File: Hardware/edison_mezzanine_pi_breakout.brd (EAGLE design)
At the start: 30.5 x 44.5 mm, 44 parts, among them U1 PCA9306, U2 EDISON_CONNECTOR_FULLMOUNTING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, U3 EDISON_CONNECTOR_FULLHEADER, U4 TPS62065, U5 MIC5219 3.3V

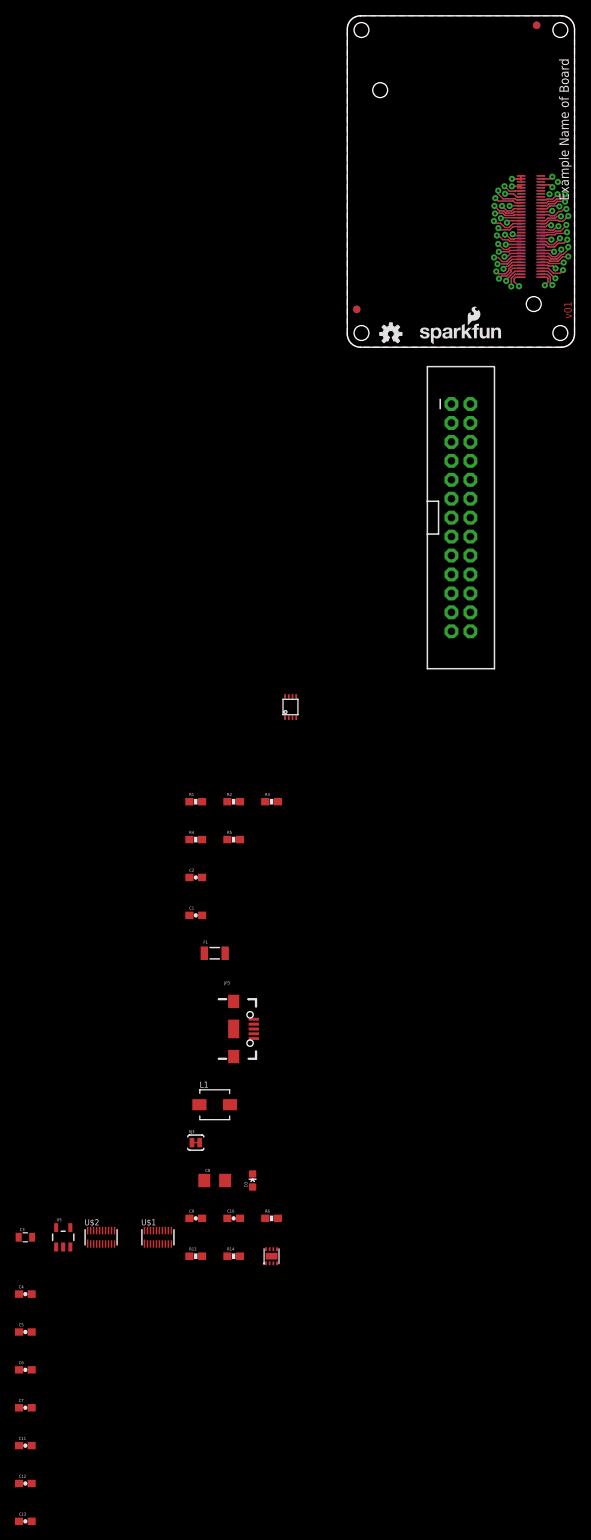
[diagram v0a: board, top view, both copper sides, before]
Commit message: Initial component placement.
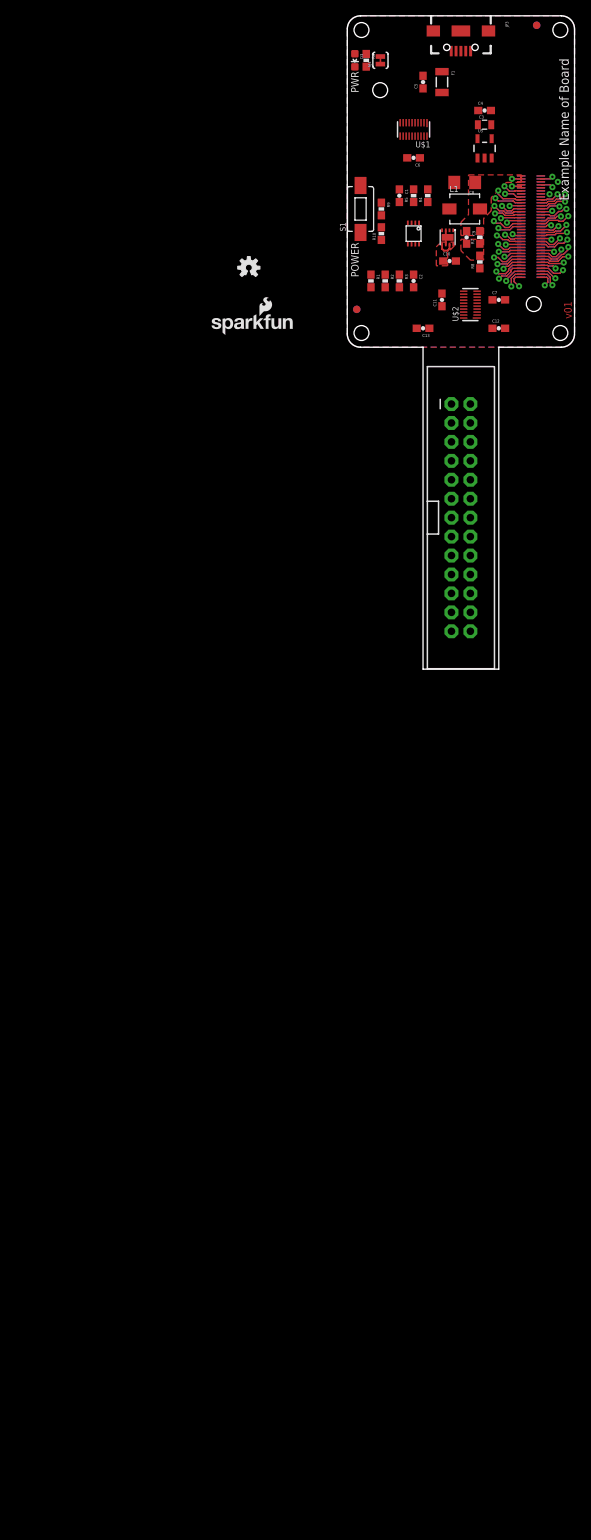
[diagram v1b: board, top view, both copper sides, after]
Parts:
- removed R13: 680k, SparkFun-Resistors:0603-RES
- removed R14: 120k, SparkFun-Resistors:0603-RES
- added R10: 22, SparkFun-Resistors:0603-RES
- added R7: 680k, SparkFun-Resistors:0603-RES
- added R8: 120k, SparkFun-Resistors:0603-RES
- added R9: 10K, SparkFun-Resistors:0603-RES
- added S1: POWER, SparkFun-Electromechanical:TACTILE-SWITCH-1101NE
- moved C5 175.9 mm to (10.2, 35.6), turned to 90 degrees
- moved C6 170.7 mm to (8.89, 25.4), turned to 180 degrees
- moved C4 170.3 mm to (18.4, 31.8)
- moved C13 168.7 mm to (10.2, 2.54), turned to 180 degrees
- moved C12 167.4 mm to (20.3, 2.54)
- moved C11 163.5 mm to (12.7, 6.35), turned to 90 degrees
- moved C7 161.6 mm to (20.3, 6.35)
- moved C3 161.4 mm to (18.4, 29.8)
- moved U5 156.6 mm to (18.4, 26.7)
- moved R6 155.8 mm to (2.54, 38.5), turned to 270 degrees
- moved U$1 152.5 mm to (8.89, 29.2), turned to 180 degrees
- moved D3 150.9 mm to (1.02, 38.5), turned to 180 degrees
- moved SJ3 147.3 mm to (4.45, 38.5), turned to 90 degrees
- moved U4 138.7 mm to (13.5, 14.7), turned to 180 degrees
- moved C8 138.0 mm to (15.7, 22.1), turned to 180 degrees
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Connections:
- new net N$15: R10.2, R9.2, S1.P$1
- net GND: now also R8.1, S1.P$2; no longer R14.1
- net N$18: now also R7.1, R8.2; no longer R13.1, R14.2
- net PWRBTN#: now also R10.1
- net VSYS: now also R7.2, R9.1; no longer R13.2
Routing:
- net 5V: track 0.00 -> 2.37 mm
- net GND: track 0.00 -> 2.11 mm
- added copper zone on layer 1, net 5V
- added copper zone on layer 1, net N$18
- added copper zone on layer 1, net VSYS
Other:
- board size 30.5 x 44.5 mm -> 30.5 x 87.6 mm
- board text added: "POWER"
- board text added: "PWR"
- board text added: "Shawn Hymel"
- board text removed: "Engineer"

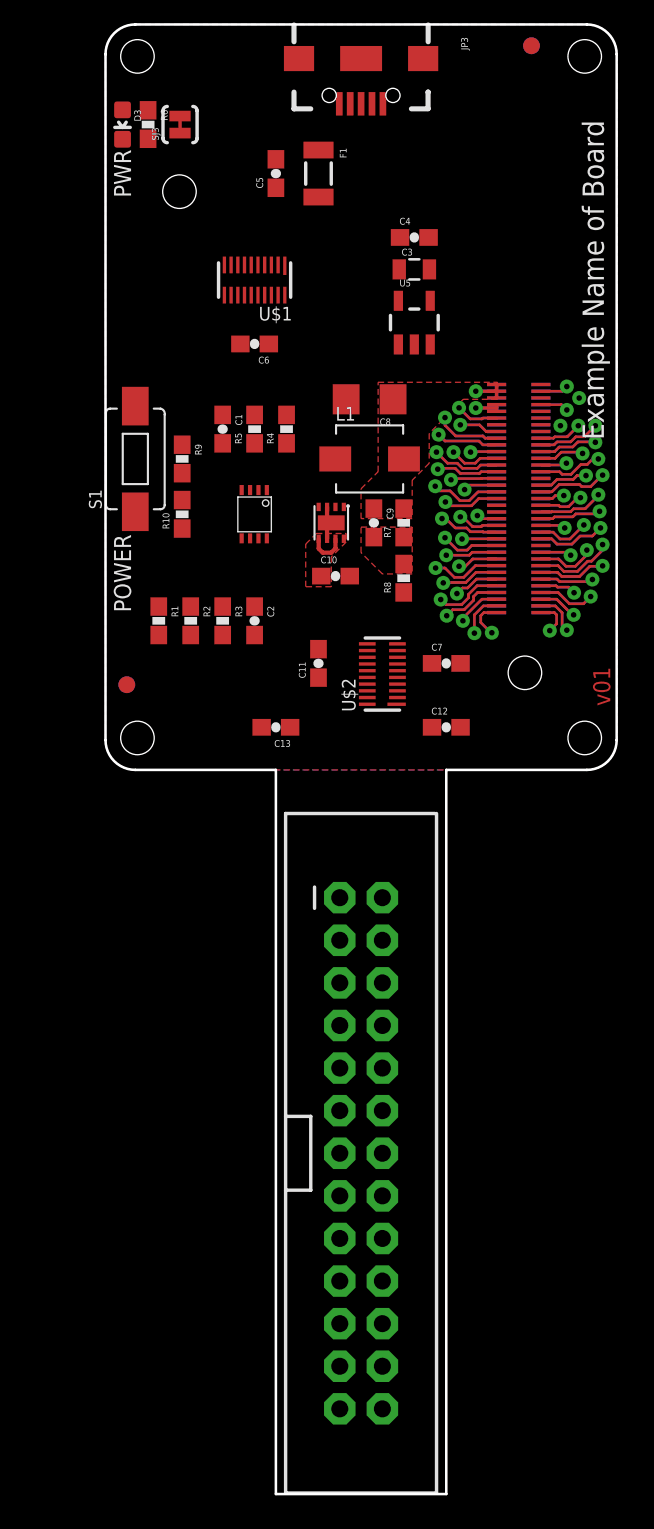
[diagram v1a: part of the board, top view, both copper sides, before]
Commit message: More layout. Swapped 22 Ohm with 220 Ohm in schematic for power button.
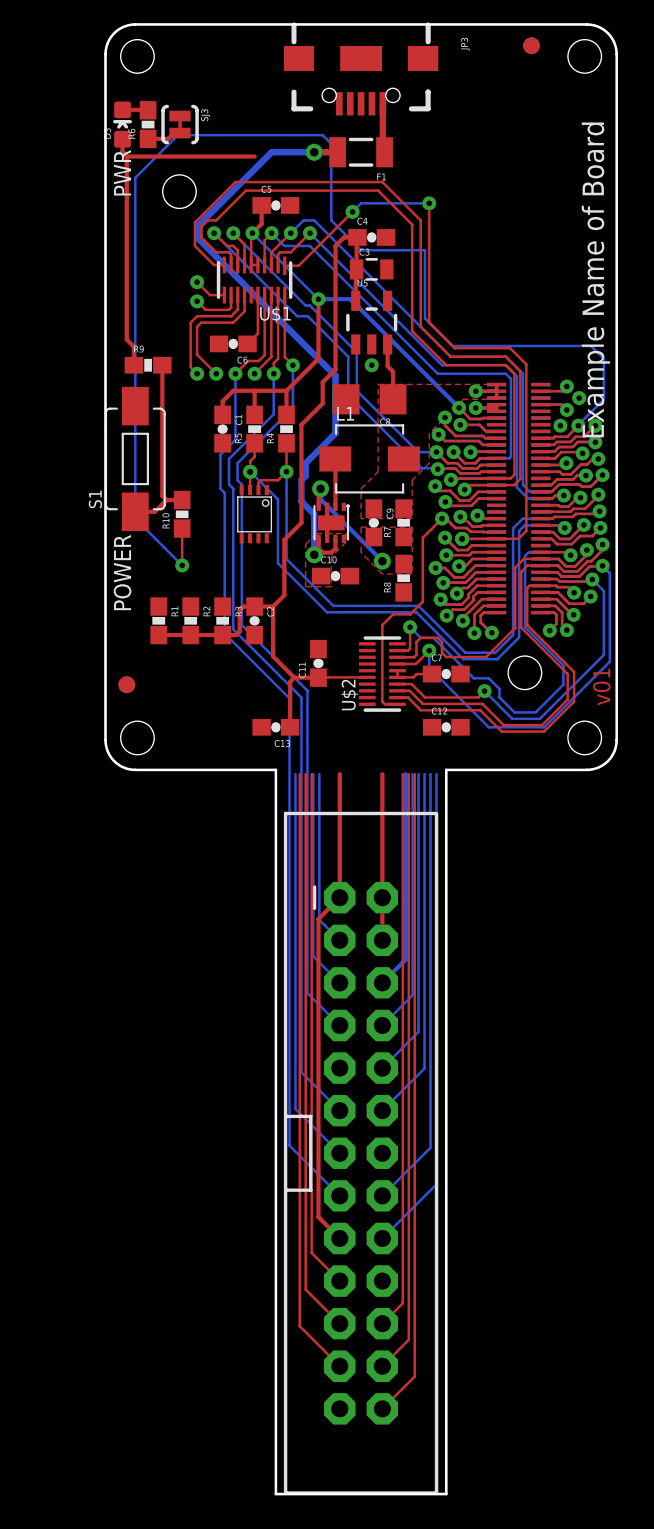
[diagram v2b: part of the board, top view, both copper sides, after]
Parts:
- R10: value 22 -> 220
- moved R9 5.95 mm to (2.54, 24.1), turned to 0 degrees
- moved F1 2.84 mm to (15.2, 36.8), turned to 180 degrees
- moved C3 2.54 mm to (15.9, 29.8)
- moved C4 2.54 mm to (15.9, 31.8)
- moved U5 2.54 mm to (15.9, 26.7)
- moved C5 1.91 mm to (10.2, 33.7), turned to 0 degrees
- moved C6 1.27 mm to (7.62, 25.4)
- moved C7 0.63 mm to (20.3, 5.71)
- turned D3 to 0 degrees
- turned R6 to 90 degrees
- turned SJ3 to 270 degrees
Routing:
- net 3.3V_LOCAL: track 0.00 -> 80.7 mm
- net PWRBTN#: track 5.08 -> 75.7 mm, vias 1 -> 2
- net PI_GP22: track 0.00 -> 58.1 mm, vias 0 -> 1
- net PI_GP17: track 0.00 -> 52.6 mm, vias 0 -> 1
- net PI_GP4: track 0.00 -> 47.6 mm, vias 0 -> 1
- net 5V: track 2.37 -> 46.5 mm, vias 0 -> 2
- net GP48: track 4.04 -> 44.5 mm
- net PI_CE1: track 0.00 -> 38.6 mm
- net GP47: track 5.51 -> 43.9 mm
- net 1.8V: track 5.07 -> 42.4 mm, vias 1 -> 3
- net PI_GP25: track 0.00 -> 36.3 mm, vias 0 -> 1
- net PI_SCLK: track 0.00 -> 36.3 mm
- net PI_GP24: track 0.00 -> 36.2 mm, vias 0 -> 1
- net GP14: track 4.13 -> 40.1 mm, vias 1 -> 4
- net PI_CE0: track 0.00 -> 36.0 mm
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
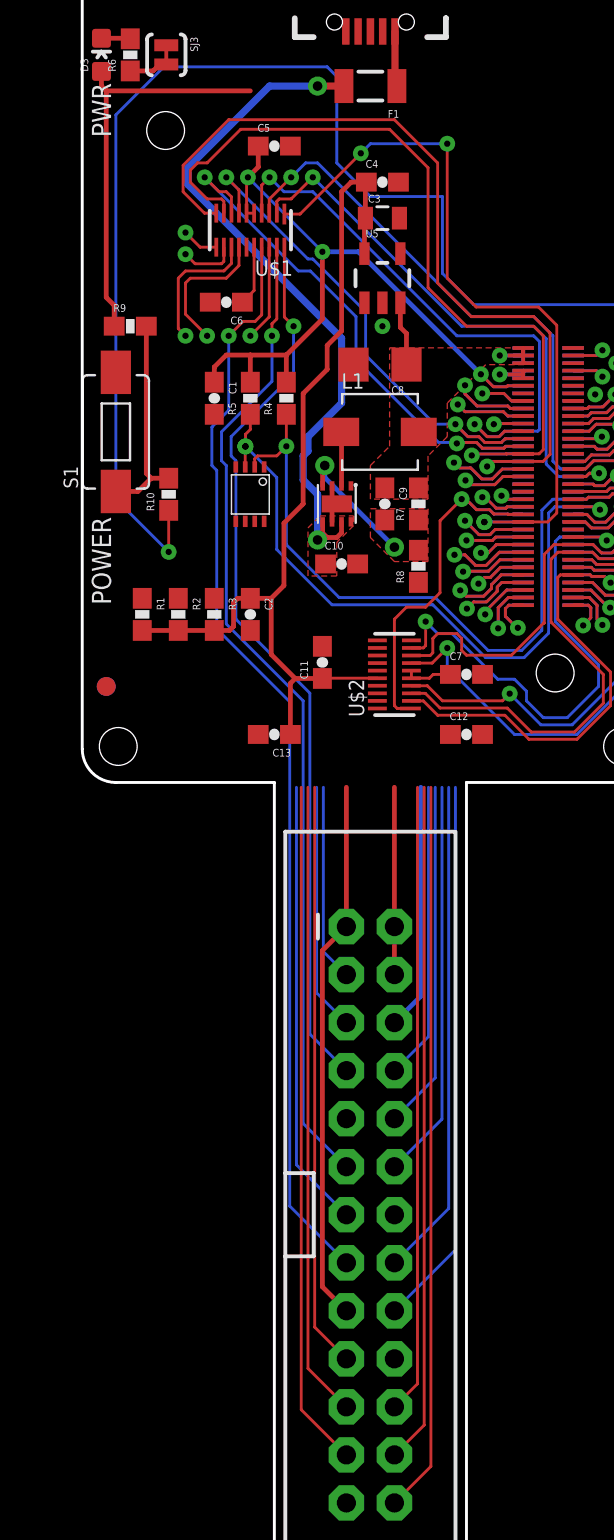
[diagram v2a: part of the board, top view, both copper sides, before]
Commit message: Added more layout to Pi connector.
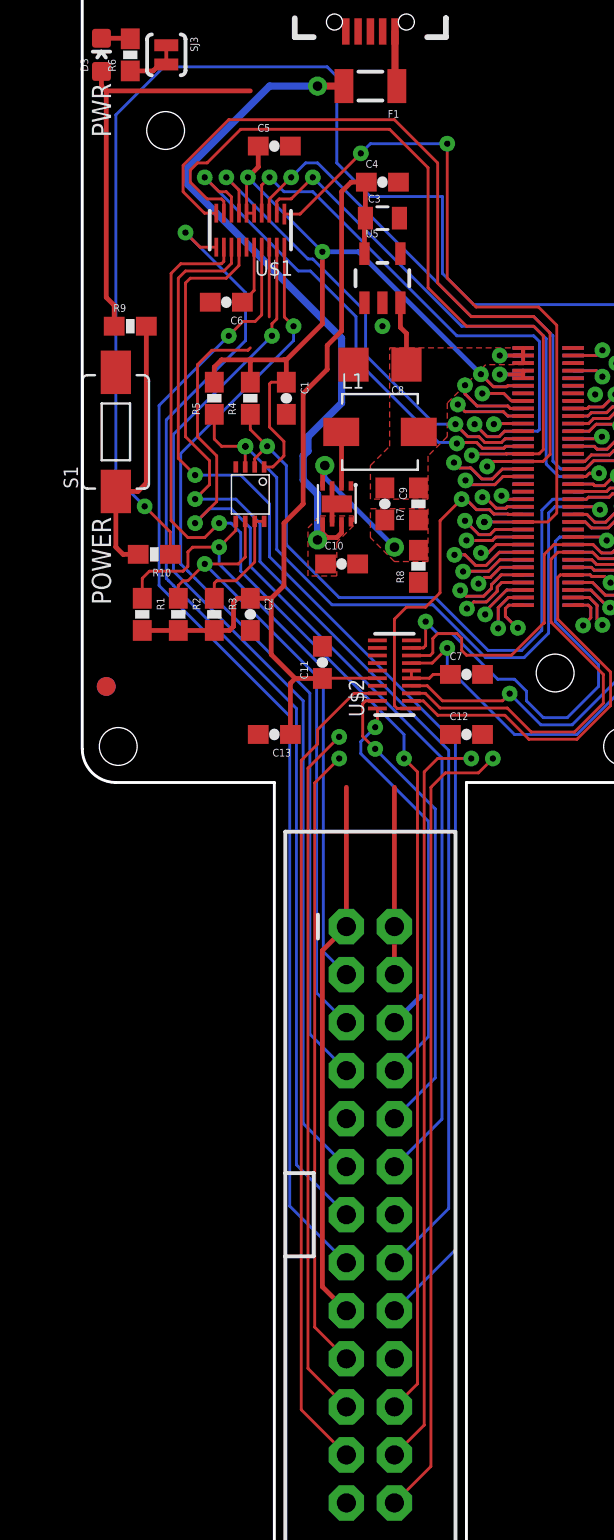
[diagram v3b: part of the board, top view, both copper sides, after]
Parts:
- moved C1 3.81 mm to (10.8, 20.3)
- moved R10 3.27 mm to (3.81, 12.1), turned to 180 degrees
- moved R5 1.91 mm to (6.99, 20.3)
- moved R4 1.90 mm to (8.89, 20.3)
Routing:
- net PI_GP25: track 36.3 -> 72.1 mm, vias 1 -> 2
- net PI_GP27: track 25.6 -> 60.9 mm
- net PI_GP18#: track 26.2 -> 58.8 mm
- net PI_GP24: track 36.2 -> 67.4 mm
- net PI_GP23: track 33.8 -> 64.8 mm
- net HV_SDA: track 10.4 -> 33.4 mm, vias 0 -> 1
- net HV_SCL: track 13.1 -> 34.1 mm, vias 0 -> 1
- net GND: track 15.1 -> 4.08 mm
- net PI_SCLK: track 36.3 -> 43.7 mm
- net PI_RXI: track 18.4 -> 25.3 mm, vias 0 -> 1
- net N$1: track 0.00 -> 6.05 mm
- net 1.8V: track 42.4 -> 48.5 mm
- net PI_TXO: track 15.7 -> 21.7 mm, vias 0 -> 1
- net PI_CE1: track 38.6 -> 42.6 mm, vias 0 -> 1
- net PI_CE0: track 36.0 -> 39.6 mm, vias 0 -> 1
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
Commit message: More layout.
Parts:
- moved C11 1.27 mm to (11.4, 6.35)
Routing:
- net 5V: track 46.5 -> 65.7 mm, vias 2 -> 4
- net PI_CE0: track 39.6 -> 55.5 mm, vias 1 -> 2
- net PI_CE1: track 42.6 -> 58.1 mm, vias 1 -> 2
- net PI_MOSI: track 33.0 -> 43.4 mm, vias 1 -> 2
- net 3.3V_LOCAL: track 80.7 -> 87.3 mm, vias 0 -> 1
- net PI_MISO: track 37.0 -> 41.2 mm, vias 1 -> 2
- net PI_GP25: track 72.1 -> 74.7 mm
- net PI_GP18#: track 58.8 -> 60.3 mm
- net PI_GP23: track 64.8 -> 66.3 mm
- net PI_GP22: track 60.4 -> 61.8 mm
- net PI_GP24: track 67.4 -> 68.8 mm
- net PI_GP27: track 60.9 -> 62.1 mm
- net PI_GP17: track 54.7 -> 55.7 mm
- net PI_GP4: track 49.9 -> 50.7 mm
- net HV_SCL: track 34.1 -> 34.8 mm
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
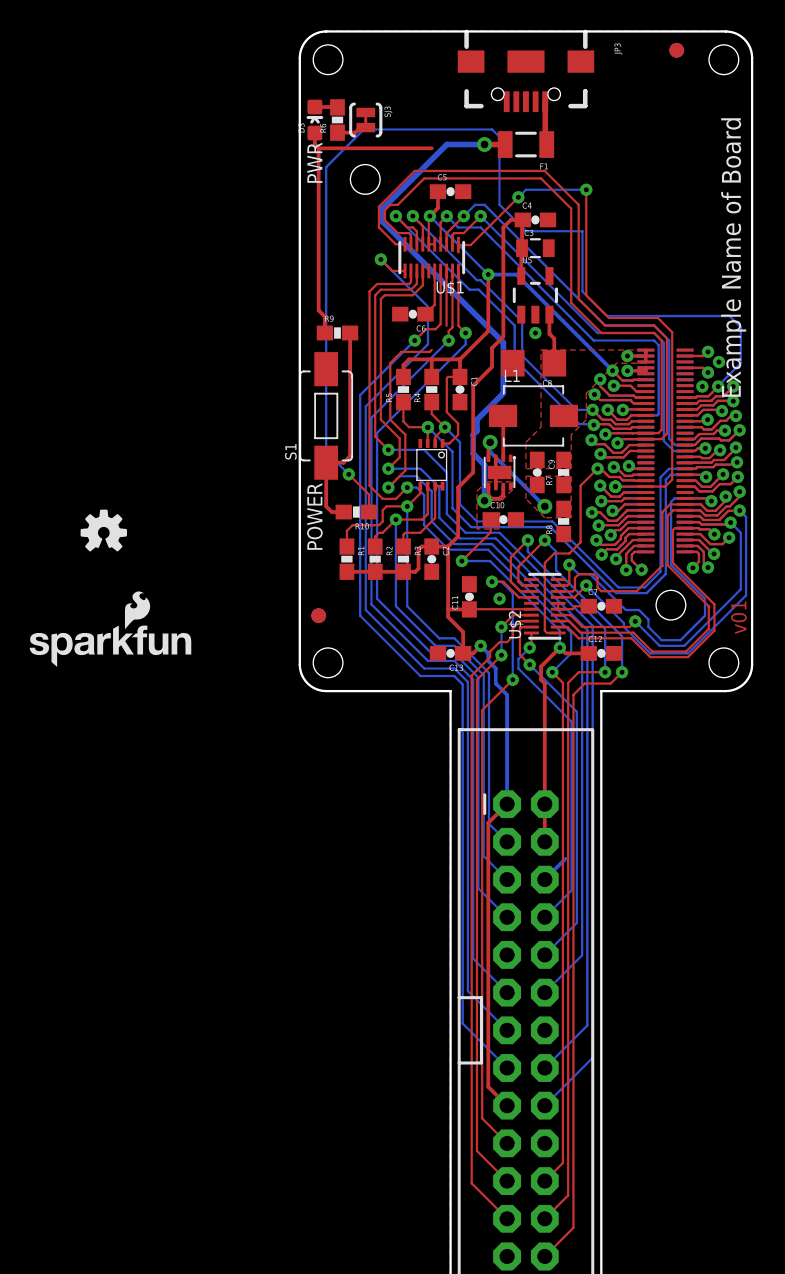
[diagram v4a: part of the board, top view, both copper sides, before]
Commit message: Finished layout for prototype.
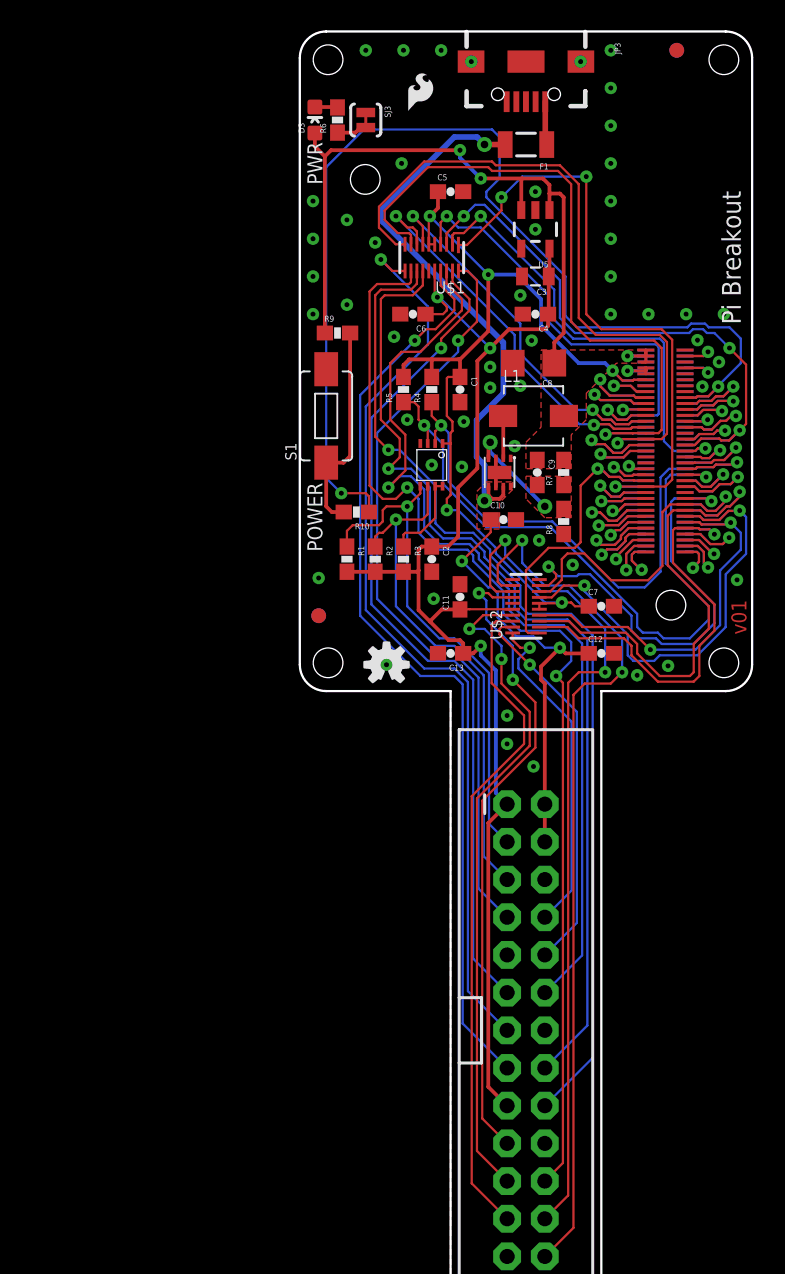
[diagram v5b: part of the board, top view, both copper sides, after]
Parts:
- LOGO3: value SFE_LOGO_NAME_FLAME.1_INCH -> SFE_LOGO_FLAME.1_INCH; device SparkFun-Aesthetics:SFE_LOGO_NAME_FLAME_.1 -> SparkFun-Aesthetics:SFE_LOGO_FLAME_.1
- moved LOGO3 41.0 mm to (6.99, 38.7), flipped to the top
- moved LOGO4 39.7 mm to (21.1, 0.25), flipped to the bottom
- moved LOGO1 21.0 mm to (5.84, 1.78)
- moved C4 6.35 mm to (15.9, 25.4), turned to 180 degrees
- moved U5 4.44 mm to (15.9, 31.1), turned to 180 degrees
- moved C3 1.90 mm to (15.9, 27.9), turned to 180 degrees
- moved U$2 1.27 mm to (15.2, 5.71)
- moved C11 0.63 mm to (10.8, 6.35)
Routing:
- net VSYS: track 29.3 -> 51.2 mm, vias 1 -> 3
- net 1.8V: track 48.5 -> 65.7 mm, vias 3 -> 5
- net GP20_I2C_1_SDA: track 38.6 -> 46.9 mm, vias 3 -> 2
- net GP13_PWM1: track 36.6 -> 40.9 mm, vias 2 -> 3
- net GP130_UART_1_RX: track 25.2 -> 29.4 mm
- net GP109_SPI_2_CLK: track 31.1 -> 35.2 mm
- net PI_MISO: track 41.2 -> 45.1 mm
- net PI_GP18#: track 60.3 -> 63.9 mm
- net GP111_SPI_2_FS1: track 27.7 -> 31.1 mm
- net GP115_SPI_2_TXD: track 31.1 -> 34.1 mm
- net 3.3V_LOCAL: track 87.3 -> 89.5 mm, vias 1 -> 3
- net GP14: track 40.1 -> 42.3 mm, vias 4 -> 3
- net GP47: track 43.9 -> 46.0 mm
- net GND: track 4.08 -> 2.11 mm, vias 4 -> 51
- net GP48: track 44.5 -> 46.4 mm
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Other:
- board text added: "Pi Breakout"
- board text removed: "Example Name of Board"
